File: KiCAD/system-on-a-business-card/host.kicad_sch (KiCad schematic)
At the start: 27 parts, among them Q1 2N7002K, Q2 2N7002K, SW2 SW_Push, U2 ESP32-C3, U3 ZD25WQ32C, Y1 40MHz

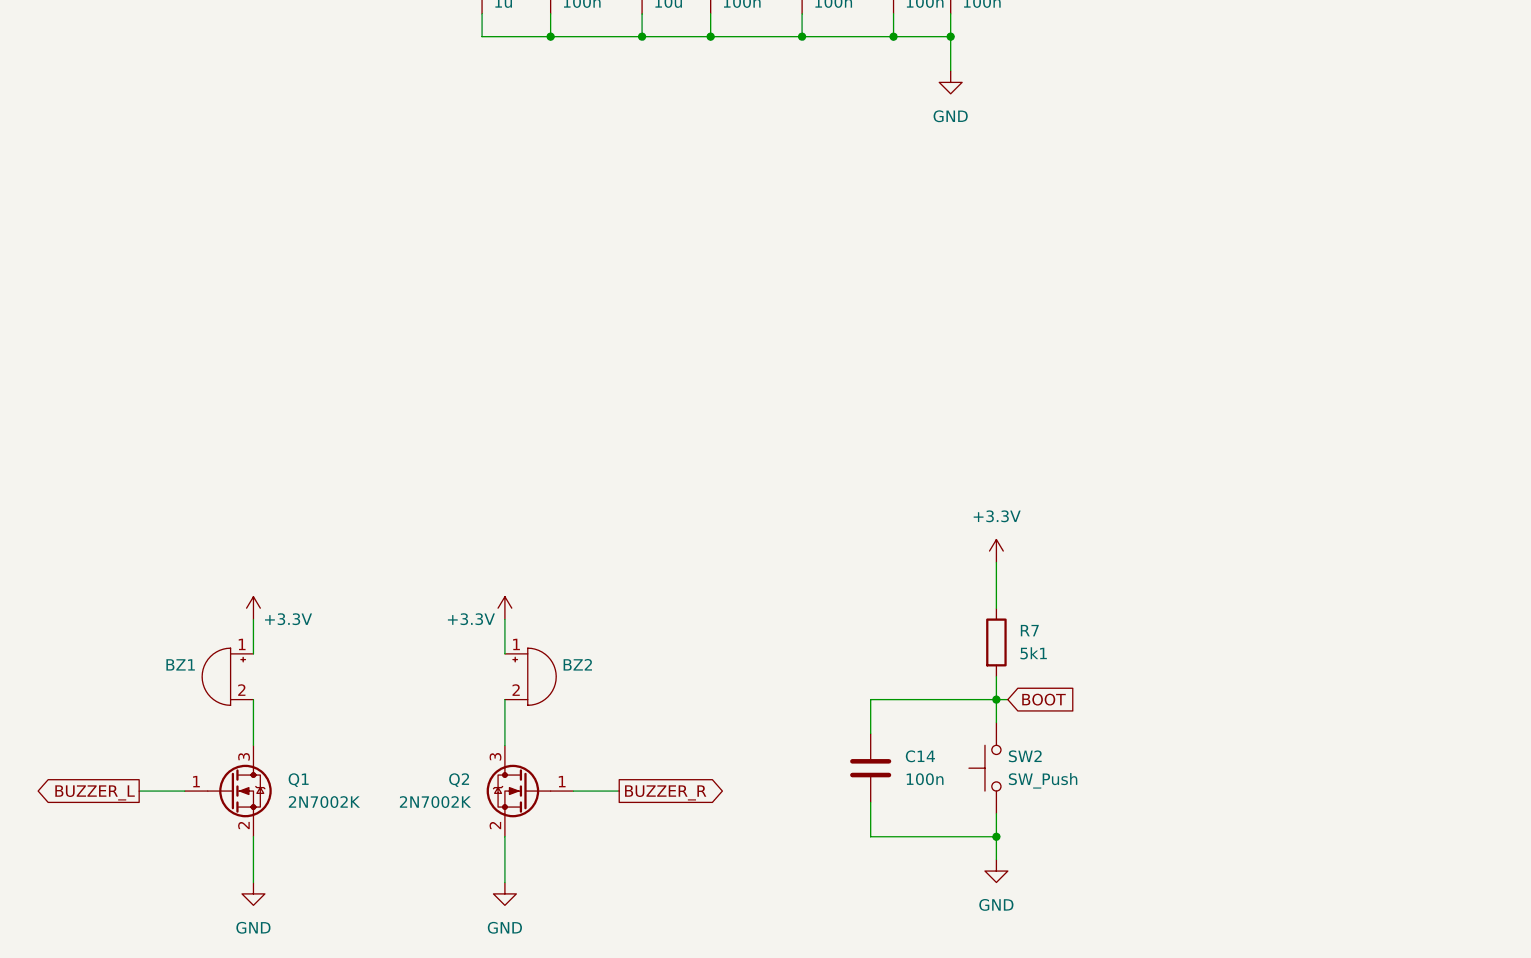
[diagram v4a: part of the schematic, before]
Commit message: #10: mintor tweaks in routing, removed fiducials from bom, added values to buzzer and sd-card slot
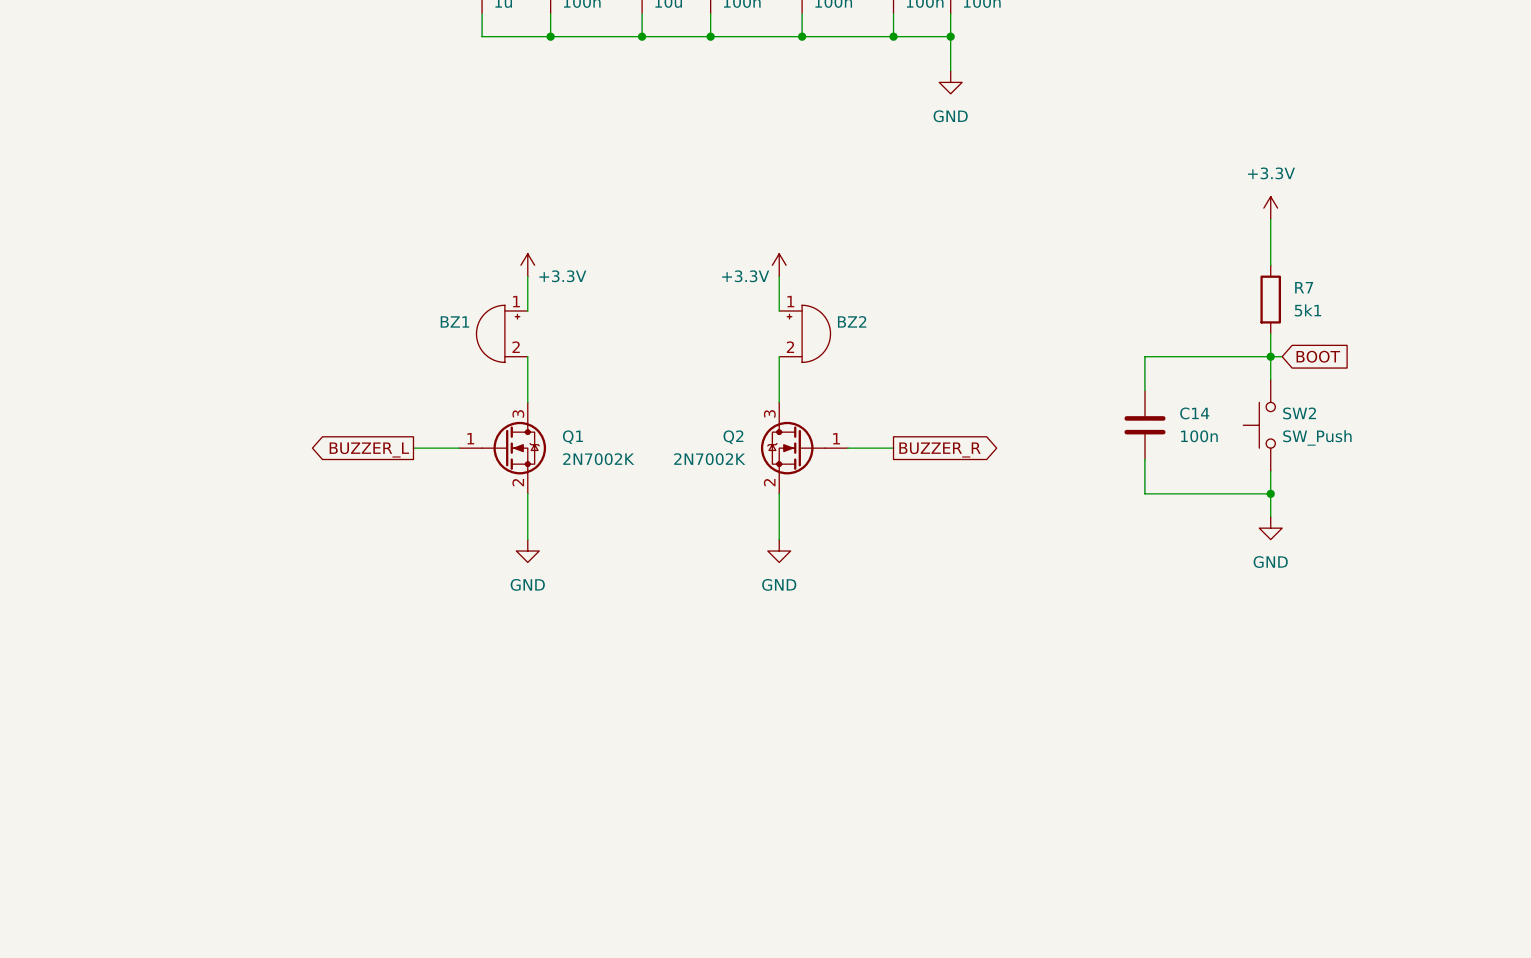
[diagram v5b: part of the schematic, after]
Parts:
- BZ1, BZ2: value Buzzer -> MLT-7525
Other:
- moved on the sheet: BZ1, BZ2, C14, Q1, Q2, R7, SW2

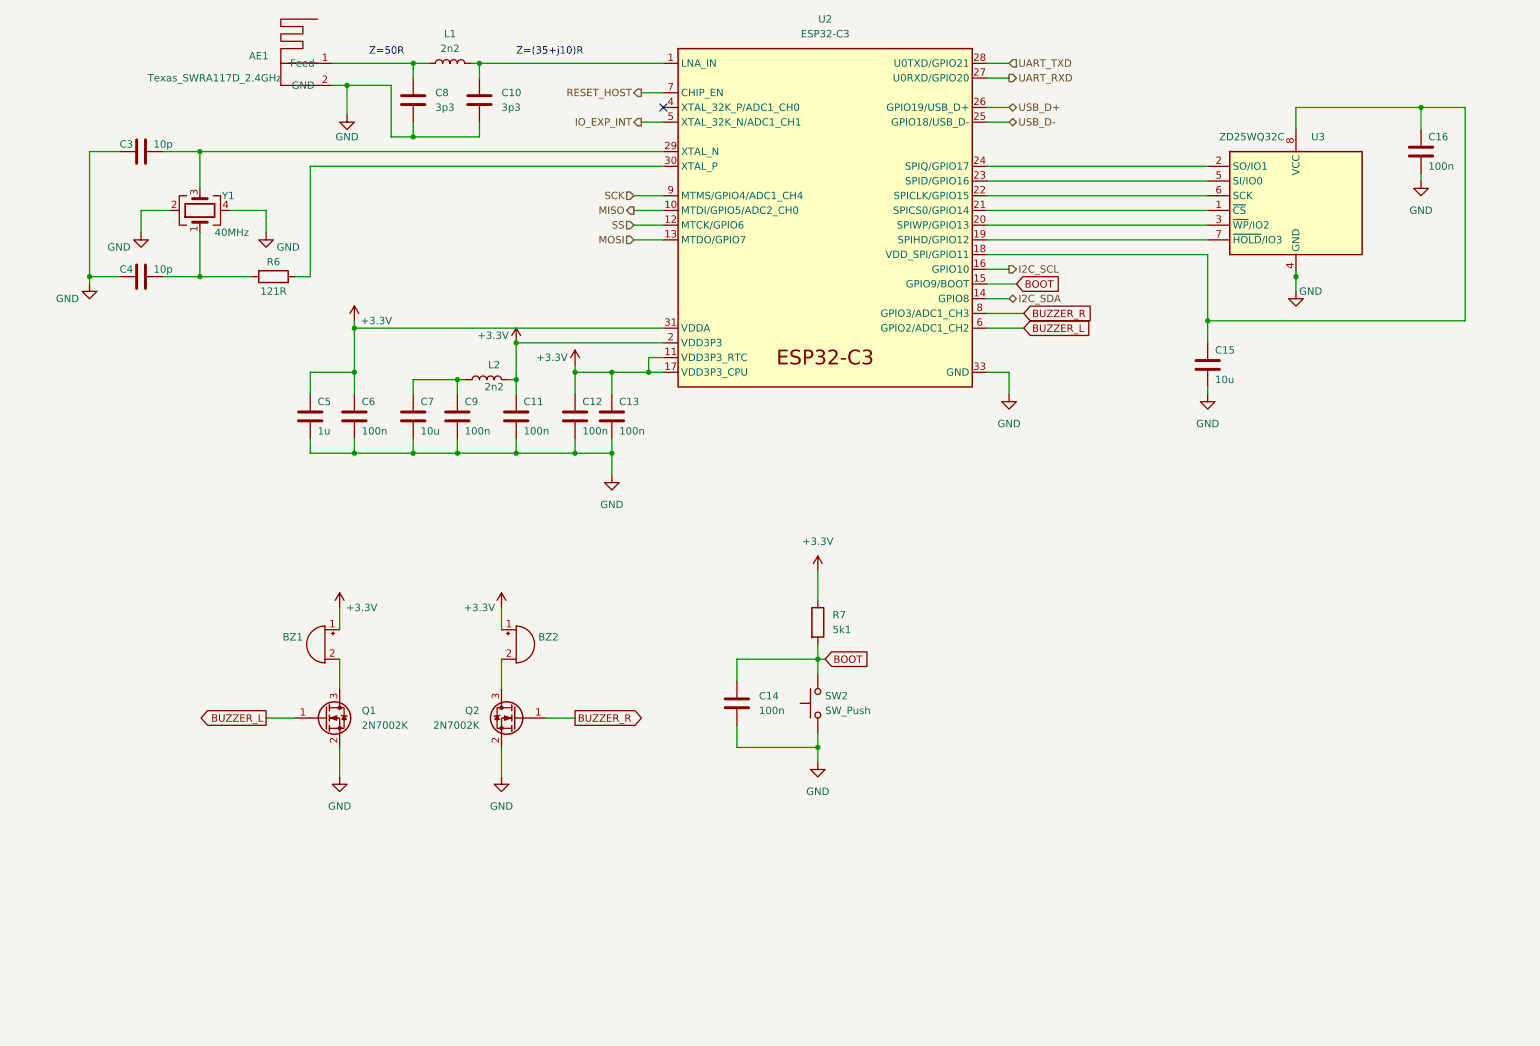
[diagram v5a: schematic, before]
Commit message: #10: created version with DAC, Op Amp and speaker
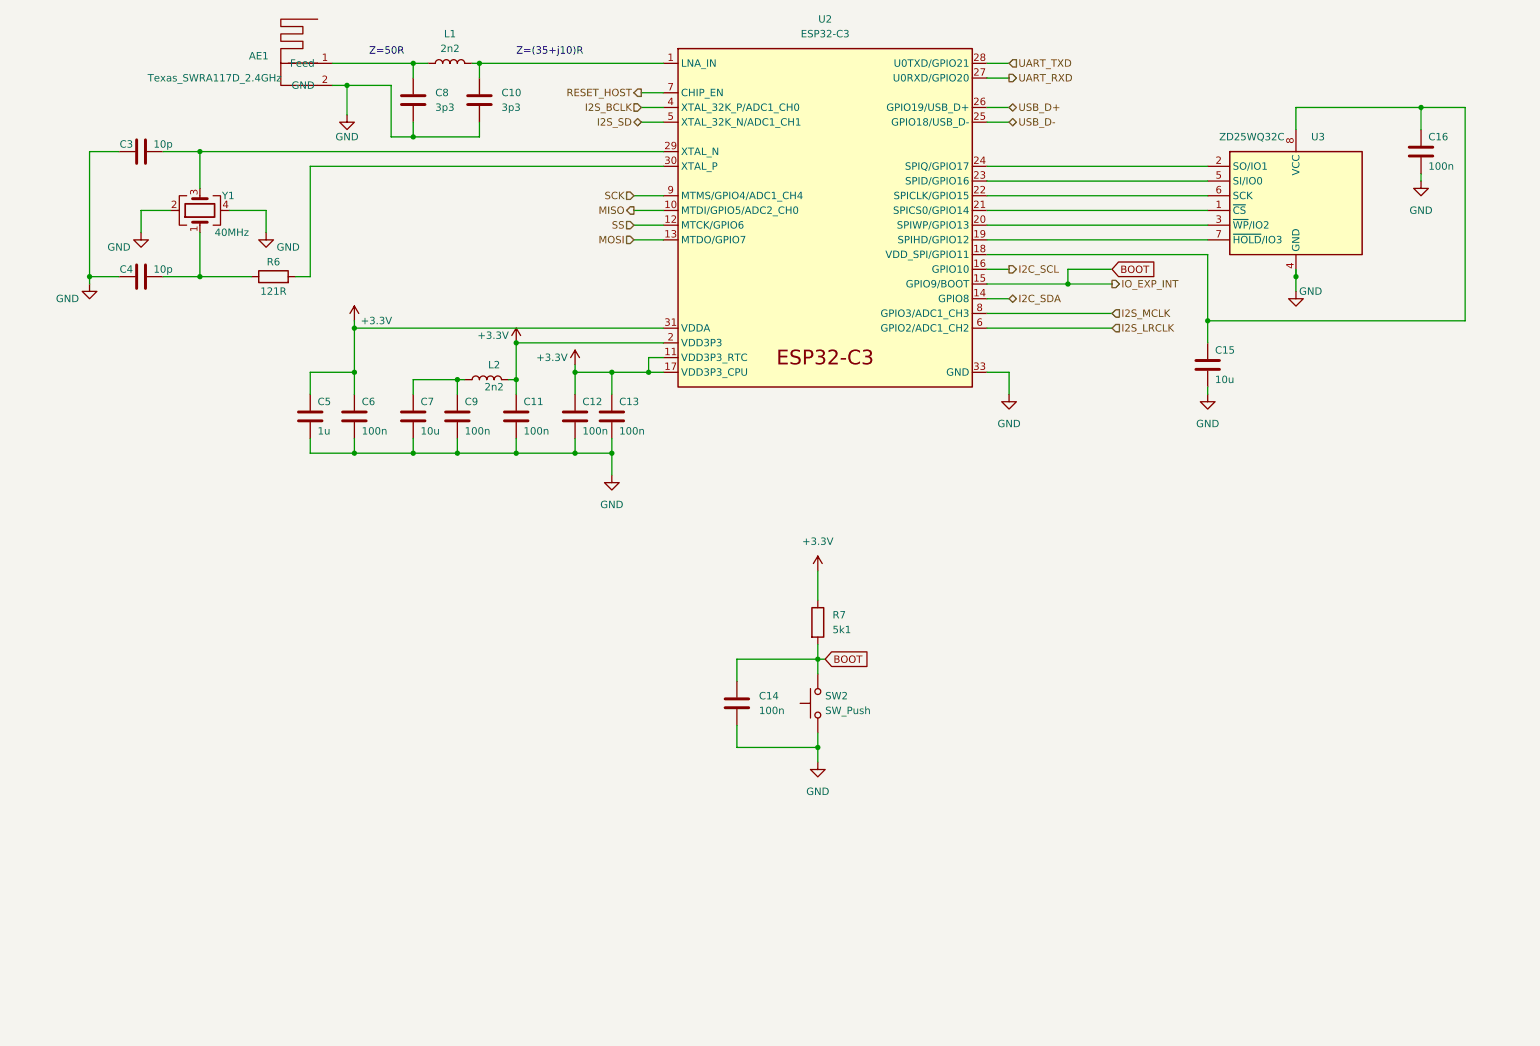
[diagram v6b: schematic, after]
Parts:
- removed BZ1, BZ2: MLT-7525, Buzzer_Beeper:MagneticBuzzer_CUI_CMT-8504-100-SMT, symbol Device:Buzzer
- removed Q1, Q2: 2N7002K, Package_TO_SOT_SMD:SOT-23, symbol Transistor_FET:2N7002K
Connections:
- net I2S_BCLK: now reaches U2.4 (XTAL_32K_P/ADC1_CH0)
- net BUZZER_L renamed I2S_LRCLK
- net BUZZER_R renamed I2S_MCLK
- net IO_EXP_INT renamed I2S_SD
- no-connect marks 1 -> 0
